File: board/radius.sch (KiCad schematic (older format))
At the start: 11 parts, among them IC1 STM8S003F3P, P1 CONN_01X04, P2 CONN_01X10, U1 CH340G, U2 LM2931AZ-3.3/5.0, Y1 Crystal

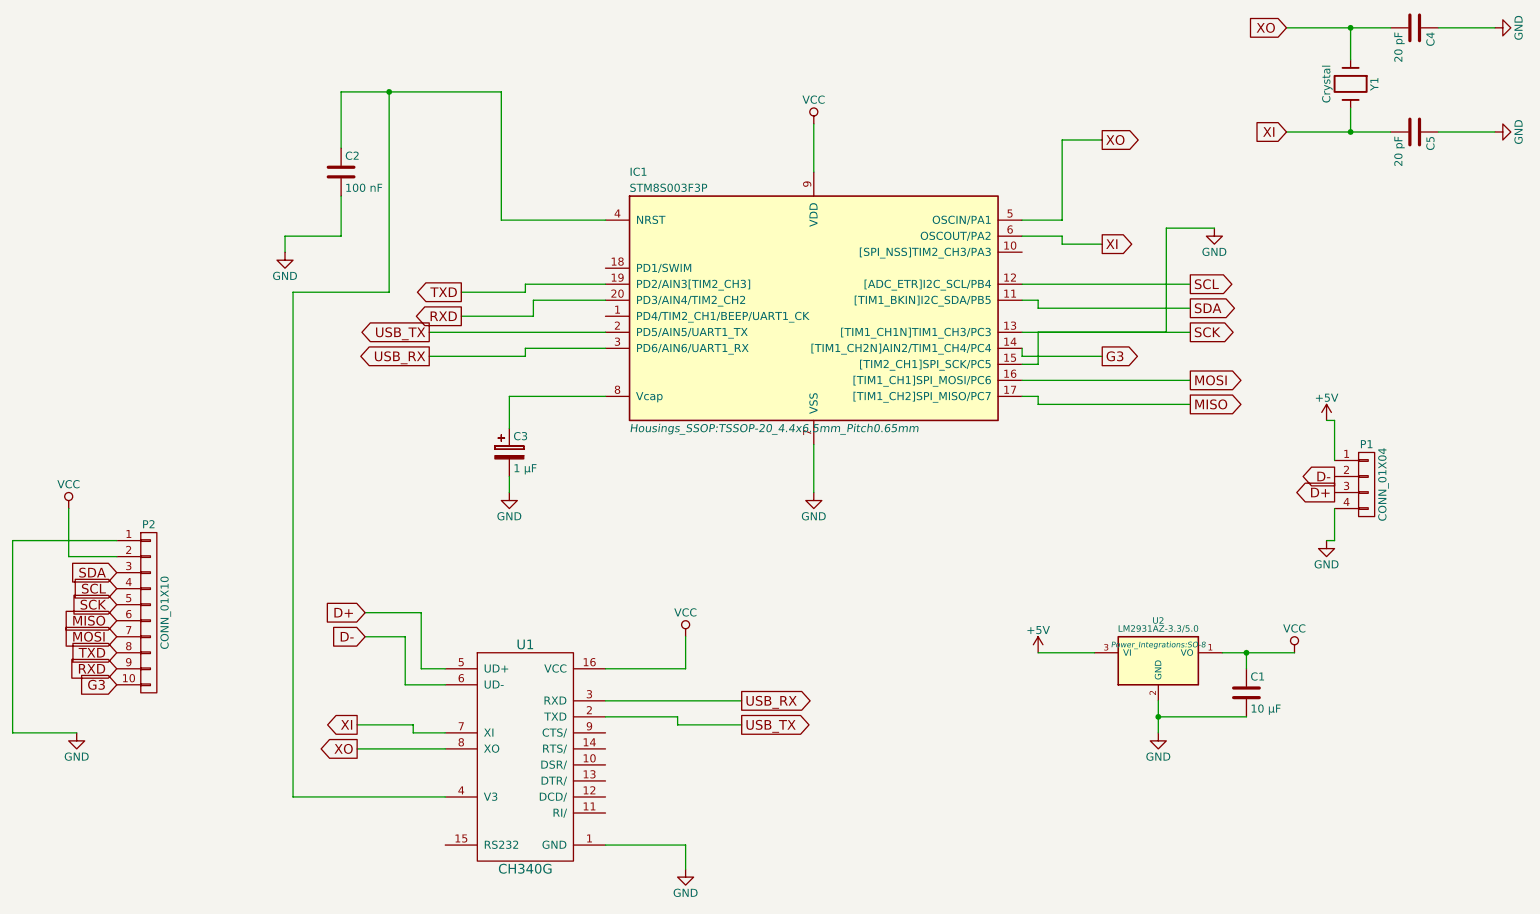
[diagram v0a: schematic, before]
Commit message: Support SWIM connector.
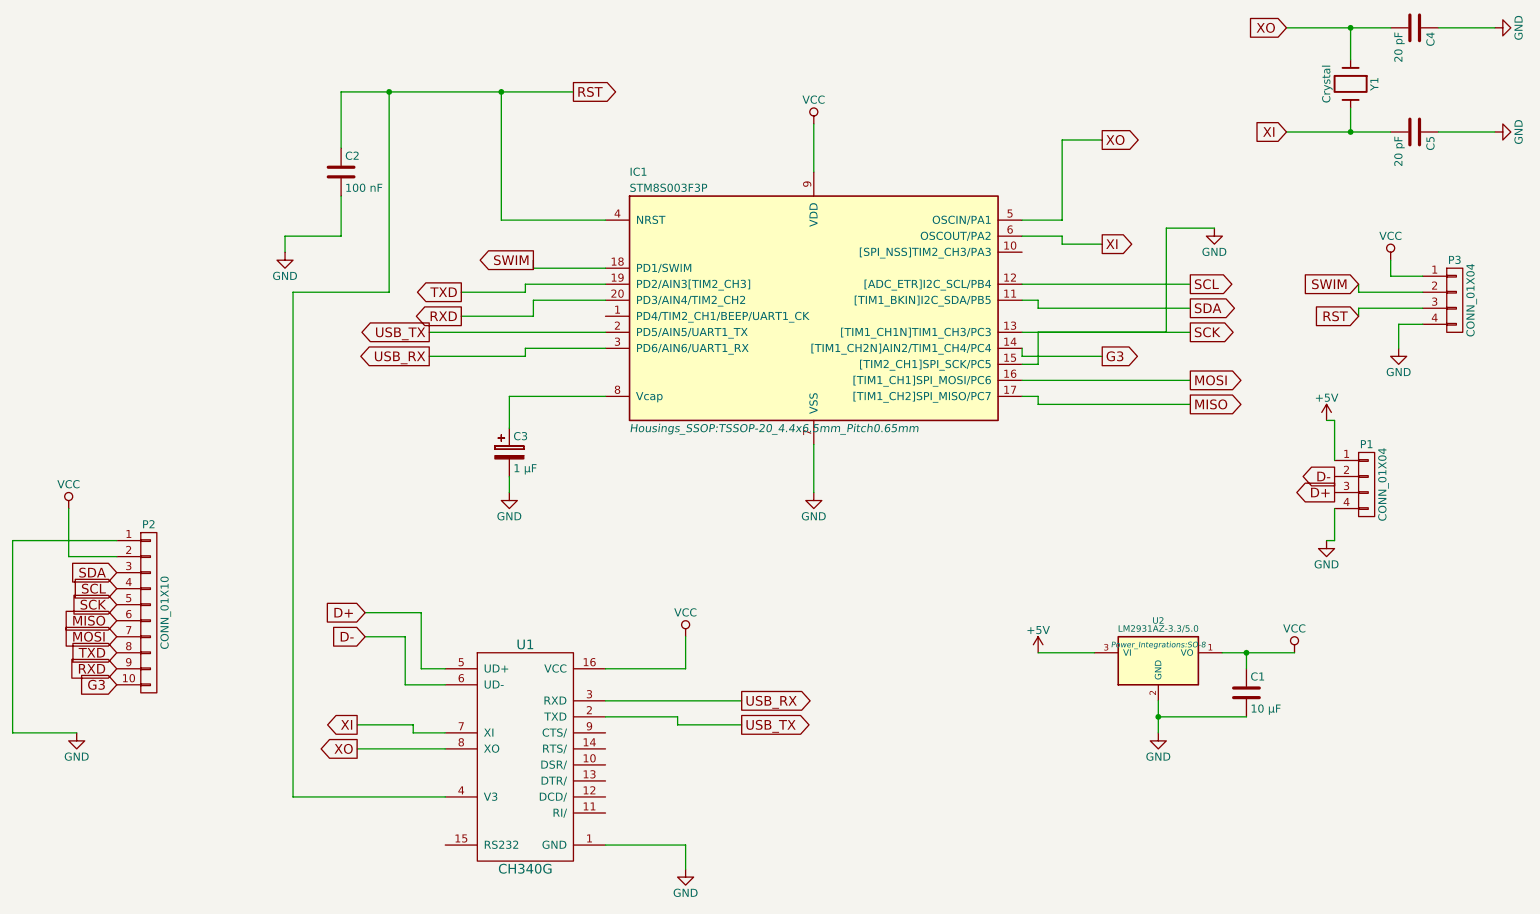
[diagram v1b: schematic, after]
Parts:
- added P3: CONN_01X04, conn-2mm:CONN-2MM-M-1x4, symbol CONN_01X04
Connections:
- net GND: now also P3.4 (P4)
- net VCC: now also P3.1 (P1)
- net SWIM: now reaches IC1.18 (PD1/SWIM)
- net SWIM: now also P3.2 (P2)
- net RST: now reaches C2.1, IC1.4 (NRST), U1.4 (V3)
- net RST: now also P3.3 (P3)
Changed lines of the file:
@@
 $EndComp
 $Comp
-L GND #PWR01
+L GND #PWR4
 U 1 1 557FA54B
 P 4100 3900
-F 0 "#PWR01" H 4100 3650 50  0001 C CNN
+F 0 "#PWR4" H 4100 3650 50  0001 C CNN
 F 1 "GND" H 4100 3750 50  0000 C CNN
 F 2 "" H 4100 3900 60  0000 C CNN
@@
 $EndComp
 $Comp
-L GND #PWR02
+L GND #PWR8
 U 1 1 557FB0DB
 P 6000 3900
-F 0 "#PWR02" H 6000 3650 50  0001 C CNN
+F 0 "#PWR8" H 6000 3650 50  0001 C CNN
 F 1 "GND" H 6000 3750 50  0000 C CNN
 F 2 "" H 6000 3900 60  0000 C CNN
@@
 $EndComp
 $Comp
-L GND #PWR03
+L GND #PWR3
 U 1 1 557FB357
 P 2700 2400
-F 0 "#PWR03" H 2700 2150 50  0001 C CNN
+F 0 "#PWR3" H 2700 2150 50  0001 C CNN
 F 1 "GND" H 2700 2250 50  0000 C CNN
 F 2 "" H 2700 2400 60  0000 C CNN
@@
 $EndComp
 $Comp
-L GND #PWR04
+L GND #PWR17
 U 1 1 557FB5FD
 P 10250 1000
-F 0 "#PWR04" H 10250 750 50  0001 C CNN
+F 0 "#PWR17" H 10250 750 50  0001 C CNN
 F 1 "GND" H 10250 850 50  0000 C CNN
 F 2 "" H 10250 1000 60  0000 C CNN
@@
 $EndComp
 $Comp
-L GND #PWR05
+L GND #PWR18
 U 1 1 557FB61D
 P 10250 1650
-F 0 "#PWR05" H 10250 1400 50  0001 C CNN
+F 0 "#PWR18" H 10250 1400 50  0001 C CNN
 F 1 "GND" H 10250 1500 50  0000 C CNN
 F 2 "" H 10250 1650 60  0000 C CNN
@@
 $EndComp
 $Comp
-L GND #PWR06
+L GND #PWR6
 U 1 1 557FBE42
 P 5200 6250
-F 0 "#PWR06" H 5200 6000 50  0001 C CNN
+F 0 "#PWR6" H 5200 6000 50  0001 C CNN
 F 1 "GND" H 5200 6100 50  0000 C CNN
 F 2 "" H 5200 6250 60  0000 C CNN
@@
 $EndComp
 $Comp
-L VCC #PWR07
+L VCC #PWR5
 U 1 1 557FBEB7
 P 5200 4800
-F 0 "#PWR07" H 5200 4650 50  0001 C CNN
+F 0 "#PWR5" H 5200 4650 50  0001 C CNN
 F 1 "VCC" H 5200 4950 50  0000 C CNN
 F 2 "" H 5200 4800 60  0000 C CNN
@@
 	3050 1750 3050 1400
 Wire Wire Line
-	3050 1400 4050 1400
+	3050 1400 4500 1400
 Wire Wire Line
 	4050 1400 4050 2200
@@
 $EndComp
 $Comp
-L VCC #PWR08
+L VCC #PWR7
 U 1 1 557FCD3A
 P 6000 1600
-F 0 "#PWR08" H 6000 1450 50  0001 C CNN
+F 0 "#PWR7" H 6000 1450 50  0001 C CNN
 F 1 "VCC" H 6000 1750 50  0000 C CNN
 F 2 "" H 6000 1600 60  0000 C CNN
@@
 $EndComp
 $Comp
-L +5V #PWR09
+L +5V #PWR9
 U 1 1 557FCD60
 P 7400 4900
-F 0 "#PWR09" H 7400 4750 50  0001 C CNN
+F 0 "#PWR9" H 7400 4750 50  0001 C CNN
 F 1 "+5V" H 7400 5040 50  0000 C CNN
 F 2 "" H 7400 4900 60  0000 C CNN
@@
 $EndComp
 $Comp
-L VCC #PWR010
+L VCC #PWR12
 U 1 1 557FCD86
 P 9000 4900
-F 0 "#PWR010" H 9000 4750 50  0001 C CNN
+F 0 "#PWR12" H 9000 4750 50  0001 C CNN
 F 1 "VCC" H 9000 5050 50  0000 C CNN
 F 2 "" H 9000 4900 60  0000 C CNN
@@
 $EndComp
 $Comp
-L GND #PWR011
+L GND #PWR10
 U 1 1 557FCDAC
 P 8150 5400
-F 0 "#PWR011" H 8150 5150 50  0001 C CNN
+F 0 "#PWR10" H 8150 5150 50  0001 C CNN
 F 1 "GND" H 8150 5250 50  0000 C CNN
 F 2 "" H 8150 5400 60  0000 C CNN
@@
 D+
 $Comp
-L GND #PWR012
+L GND #PWR14
 U 1 1 557FD427
 P 9200 4200
-F 0 "#PWR012" H 9200 3950 50  0001 C CNN
+F 0 "#PWR14" H 9200 3950 50  0001 C CNN
 F 1 "GND" H 9200 4050 50  0000 C CNN
 F 2 "" H 9200 4200 60  0000 C CNN
@@
 $EndComp
 $Comp
-L +5V #PWR013
+L +5V #PWR13
 U 1 1 557FD44F
 P 9200 3450
-F 0 "#PWR013" H 9200 3300 50  0001 C CNN
+F 0 "#PWR13" H 9200 3300 50  0001 C CNN
 F 1 "+5V" H 9200 3590 50  0000 C CNN
 F 2 "" H 9200 3450 60  0000 C CNN
@@
 $EndComp
 $Comp
-L GND #PWR014
+L GND #PWR2
 U 1 1 557FD669
 P 1400 5400
-F 0 "#PWR014" H 1400 5150 50  0001 C CNN
+F 0 "#PWR2" H 1400 5150 50  0001 C CNN
 F 1 "GND" H 1400 5250 50  0000 C CNN
 F 2 "" H 1400 5400 60  0000 C CNN
@@
 $EndComp
 $Comp
-L VCC #PWR015
+L VCC #PWR1
 U 1 1 557FD693
 P 1350 4000
-F 0 "#PWR015" H 1350 3850 50  0001 C CNN
+F 0 "#PWR1" H 1350 3850 50  0001 C CNN
 F 1 "VCC" H 1350 4150 50  0000 C CNN
 F 2 "" H 1350 4000 60  0000 C CNN
@@
 	8200 2250 8500 2250
 $Comp
-L GND #PWR016
+L GND #PWR11
 U 1 1 559188A2
 P 8500 2250
-F 0 "#PWR016" H 8500 2000 50  0001 C CNN
+F 0 "#PWR11" H 8500 2000 50  0001 C CNN
 F 1 "GND" H 8500 2100 50  0000 C CNN
 F 2 "" H 8500 2250 60  0000 C CNN
@@
 	1    0    0    -1
 $EndComp
+Connection ~ 4050 1400
+Text GLabel 4500 1400 2    60   Output ~ 0
+RST
+$Comp
+L CONN_01X04 P3
+U 1 1 55AC5BB9
+P 10000 2700
+F 0 "P3" H 10000 2950 50  0000 C CNN
+F 1 "CONN_01X04" V 10100 2700 50  0000 C CNN
+F 2 "conn-2mm:CONN-2MM-M-1x4" H 10000 2700 60  0001 C CNN
+F 3 "" H 10000 2700 60  0000 C CNN
+	1    10000 2700
+	1    0    0    -1
+$EndComp
+$Comp
+L GND #PWR16
+U 1 1 55AC5C37
+P 9650 3000
+F 0 "#PWR16" H 9650 2750 50  0001 C CNN
+F 1 "GND" H 9650 2850 50  0000 C CNN
+F 2 "" H 9650 3000 60  0000 C CNN
+F 3 "" H 9650 3000 60  0000 C CNN
+	1    9650 3000
+	1    0    0    -1
+$EndComp
+$Comp
+L VCC #PWR15
+U 1 1 55AC5C63
+P 9600 2450
+F 0 "#PWR15" H 9600 2300 50  0001 C CNN
+F 1 "VCC" H 9600 2600 50  0000 C CNN
+F 2 "" H 9600 2450 60  0000 C CNN
+F 3 "" H 9600 2450 60  0000 C CNN
+	1    9600 2450
+	1    0    0    -1
+$EndComp
+Wire Wire Line
+	9800 2550 9600 2550
+Wire Wire Line
+	9600 2550 9600 2450
+Wire Wire Line
+	9800 2850 9650 2850
+Wire Wire Line
+	9650 2850 9650 3000
+Text GLabel 9400 2600 0    60   Input ~ 0
+SWIM
+Text GLabel 9400 2800 0    60   Input ~ 0
+RST
+Wire Wire Line
+	9800 2750 9400 2750
+Wire Wire Line
+	9400 2750 9400 2800
+Wire Wire Line
+	9800 2650 9400 2650
+Wire Wire Line
+	9400 2650 9400 2600
+Text GLabel 4250 2450 0    60   Output ~ 0
+SWIM
+Wire Wire Line
+	4700 2500 4250 2500
+Wire Wire Line
+	4250 2500 4250 2450
 $EndSCHEMATC

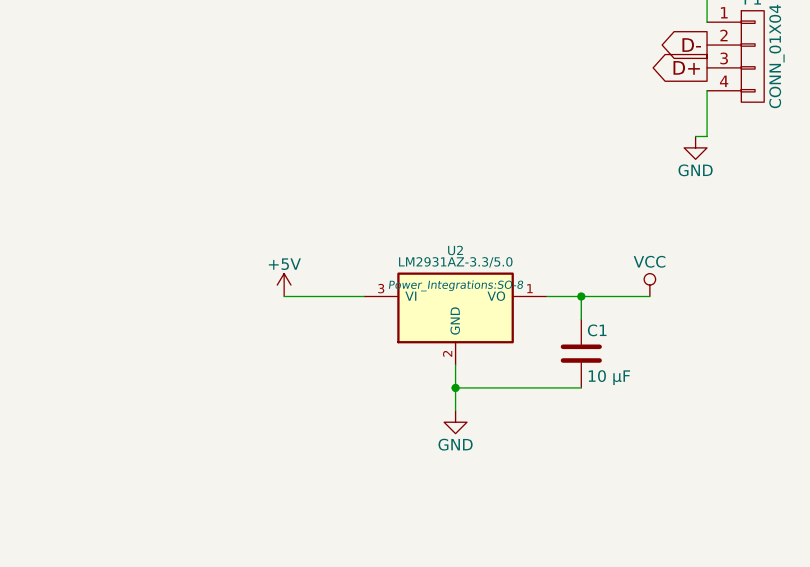
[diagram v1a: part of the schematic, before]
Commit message: Corrects power adapter pinout.
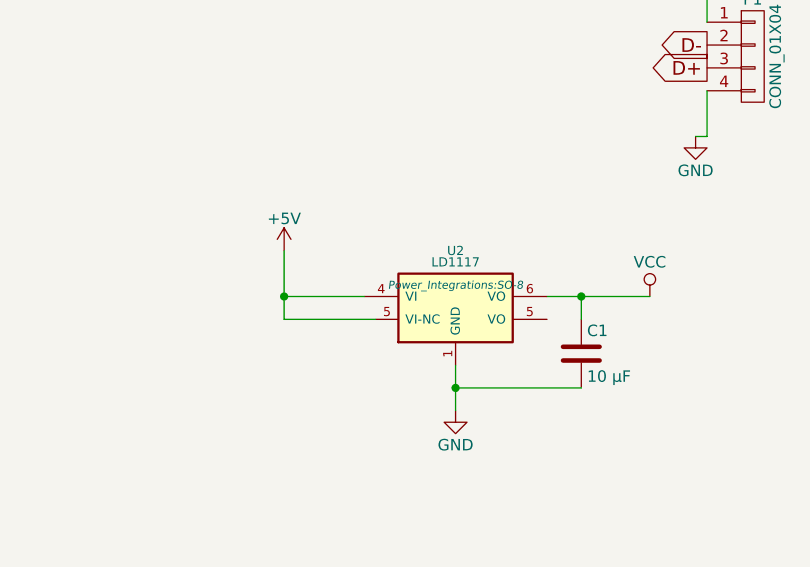
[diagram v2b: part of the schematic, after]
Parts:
- removed U2: LM2931AZ-3.3/5.0, Power_Integrations:SO-8, symbol LM2931AZ-3.3/5.0
- added U2: LD1117, Power_Integrations:SO-8, symbol LD1117
- P3: footprint conn-2mm:CONN-2MM-M-1x4 -> radius:RADIUS-CONN-2MM-M-1x4
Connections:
- net +5V: now also U2.4 (VI), U2.5 (VO)
- net GND: now also U2.1 (GND)
- net VCC: now also U2.6 (VO)
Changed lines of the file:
@@
 LIBS:stm8
 LIBS:serial_interface
-LIBS:radius-cache
+LIBS:radius
 EELAYER 25 0
 EELAYER END
@@
 $EndComp
 $Comp
-L GND #PWR4
+L GND #PWR01
 U 1 1 557FA54B
 P 4100 3900
-F 0 "#PWR4" H 4100 3650 50  0001 C CNN
+F 0 "#PWR01" H 4100 3650 50  0001 C CNN
 F 1 "GND" H 4100 3750 50  0000 C CNN
 F 2 "" H 4100 3900 60  0000 C CNN
@@
 $EndComp
 $Comp
-L GND #PWR8
+L GND #PWR02
 U 1 1 557FB0DB
 P 6000 3900
-F 0 "#PWR8" H 6000 3650 50  0001 C CNN
+F 0 "#PWR02" H 6000 3650 50  0001 C CNN
 F 1 "GND" H 6000 3750 50  0000 C CNN
 F 2 "" H 6000 3900 60  0000 C CNN
@@
 $EndComp
 $Comp
-L GND #PWR3
+L GND #PWR03
 U 1 1 557FB357
 P 2700 2400
-F 0 "#PWR3" H 2700 2150 50  0001 C CNN
+F 0 "#PWR03" H 2700 2150 50  0001 C CNN
 F 1 "GND" H 2700 2250 50  0000 C CNN
 F 2 "" H 2700 2400 60  0000 C CNN
@@
 $EndComp
 $Comp
-L GND #PWR17
+L GND #PWR04
 U 1 1 557FB5FD
 P 10250 1000
-F 0 "#PWR17" H 10250 750 50  0001 C CNN
+F 0 "#PWR04" H 10250 750 50  0001 C CNN
 F 1 "GND" H 10250 850 50  0000 C CNN
 F 2 "" H 10250 1000 60  0000 C CNN
@@
 $EndComp
 $Comp
-L GND #PWR18
+L GND #PWR05
 U 1 1 557FB61D
 P 10250 1650
-F 0 "#PWR18" H 10250 1400 50  0001 C CNN
+F 0 "#PWR05" H 10250 1400 50  0001 C CNN
 F 1 "GND" H 10250 1500 50  0000 C CNN
 F 2 "" H 10250 1650 60  0000 C CNN
@@
 $EndComp
 $Comp
-L GND #PWR6
+L GND #PWR06
 U 1 1 557FBE42
 P 5200 6250
-F 0 "#PWR6" H 5200 6000 50  0001 C CNN
+F 0 "#PWR06" H 5200 6000 50  0001 C CNN
 F 1 "GND" H 5200 6100 50  0000 C CNN
 F 2 "" H 5200 6250 60  0000 C CNN
@@
 $EndComp
 $Comp
-L VCC #PWR5
+L VCC #PWR07
 U 1 1 557FBEB7
 P 5200 4800
-F 0 "#PWR5" H 5200 4650 50  0001 C CNN
+F 0 "#PWR07" H 5200 4650 50  0001 C CNN
 F 1 "VCC" H 5200 4950 50  0000 C CNN
 F 2 "" H 5200 4800 60  0000 C CNN
@@
 	3450 4800 3200 4800
 $Comp
-L LM2931AZ-3.3/5.0 U2
-U 1 1 557FCB91
-P 8150 4950
-F 0 "U2" H 8150 5200 40  0000 C CNN
-F 1 "LM2931AZ-3.3/5.0" H 8150 5150 40  0000 C CNN
-F 2 "Power_Integrations:SO-8" H 8150 5050 35  0000 C CIN
-F 3 "" H 8150 4950 60  0000 C CNN
-	1    8150 4950
-	1    0    0    -1
-$EndComp
-$Comp
-L VCC #PWR7
+L VCC #PWR08
 U 1 1 557FCD3A
 P 6000 1600
-F 0 "#PWR7" H 6000 1450 50  0001 C CNN
+F 0 "#PWR08" H 6000 1450 50  0001 C CNN
 F 1 "VCC" H 6000 1750 50  0000 C CNN
 F 2 "" H 6000 1600 60  0000 C CNN
@@
 $EndComp
 $Comp
-L +5V #PWR9
+L +5V #PWR09
 U 1 1 557FCD60
-P 7400 4900
-F 0 "#PWR9" H 7400 4750 50  0001 C CNN
-F 1 "+5V" H 7400 5040 50  0000 C CNN
-F 2 "" H 7400 4900 60  0000 C CNN
-F 3 "" H 7400 4900 60  0000 C CNN
-	1    7400 4900
-	1    0    0    -1
-$EndComp
-$Comp
-L VCC #PWR12
+P 7400 4700
+F 0 "#PWR09" H 7400 4550 50  0001 C CNN
+F 1 "+5V" H 7400 4840 50  0000 C CNN
+F 2 "" H 7400 4700 60  0000 C CNN
+F 3 "" H 7400 4700 60  0000 C CNN
+	1    7400 4700
+	1    0    0    -1
+$EndComp
+$Comp
+L VCC #PWR010
 U 1 1 557FCD86
 P 9000 4900
-F 0 "#PWR12" H 9000 4750 50  0001 C CNN
+F 0 "#PWR010" H 9000 4750 50  0001 C CNN
 F 1 "VCC" H 9000 5050 50  0000 C CNN
 F 2 "" H 9000 4900 60  0000 C CNN
@@
 $EndComp
 $Comp
-L GND #PWR10
+L GND #PWR011
 U 1 1 557FCDAC
 P 8150 5400
-F 0 "#PWR10" H 8150 5150 50  0001 C CNN
+F 0 "#PWR011" H 8150 5150 50  0001 C CNN
 F 1 "GND" H 8150 5250 50  0000 C CNN
 F 2 "" H 8150 5400 60  0000 C CNN
@@
 	1    0    0    -1
 $EndComp
-Wire Wire Line
-	7400 4900 7750 4900
 Wire Wire Line
 	8550 4900 9000 4900
@@
 D+
 $Comp
-L GND #PWR14
+L GND #PWR012
 U 1 1 557FD427
 P 9200 4200
-F 0 "#PWR14" H 9200 3950 50  0001 C CNN
+F 0 "#PWR012" H 9200 3950 50  0001 C CNN
 F 1 "GND" H 9200 4050 50  0000 C CNN
 F 2 "" H 9200 4200 60  0000 C CNN
@@
 $EndComp
 $Comp
-L +5V #PWR13
+L +5V #PWR013
 U 1 1 557FD44F
 P 9200 3450
-F 0 "#PWR13" H 9200 3300 50  0001 C CNN
+F 0 "#PWR013" H 9200 3300 50  0001 C CNN
 F 1 "+5V" H 9200 3590 50  0000 C CNN
 F 2 "" H 9200 3450 60  0000 C CNN
@@
 $EndComp
 $Comp
-L GND #PWR2
+L GND #PWR014
 U 1 1 557FD669
 P 1400 5400
-F 0 "#PWR2" H 1400 5150 50  0001 C CNN
+F 0 "#PWR014" H 1400 5150 50  0001 C CNN
 F 1 "GND" H 1400 5250 50  0000 C CNN
 F 2 "" H 1400 5400 60  0000 C CNN
@@
 $EndComp
 $Comp
-L VCC #PWR1
+L VCC #PWR015
 U 1 1 557FD693
 P 1350 4000
-F 0 "#PWR1" H 1350 3850 50  0001 C CNN
+F 0 "#PWR015" H 1350 3850 50  0001 C CNN
 F 1 "VCC" H 1350 4150 50  0000 C CNN
 F 2 "" H 1350 4000 60  0000 C CNN
@@
 	8200 2250 8500 2250
 $Comp
-L GND #PWR11
+L GND #PWR016
 U 1 1 559188A2
 P 8500 2250
-F 0 "#PWR11" H 8500 2000 50  0001 C CNN
+F 0 "#PWR016" H 8500 2000 50  0001 C CNN
 F 1 "GND" H 8500 2100 50  0000 C CNN
 F 2 "" H 8500 2250 60  0000 C CNN
@@
 F 0 "P3" H 10000 2950 50  0000 C CNN
 F 1 "CONN_01X04" V 10100 2700 50  0000 C CNN
-F 2 "conn-2mm:CONN-2MM-M-1x4" H 10000 2700 60  0001 C CNN
+F 2 "radius:RADIUS-CONN-2MM-M-1x4" H 10000 2700 60  0001 C CNN
 F 3 "" H 10000 2700 60  0000 C CNN
 	1    10000 2700
@@
 $EndComp
 $Comp
-L GND #PWR16
+L GND #PWR017
 U 1 1 55AC5C37
 P 9650 3000
-F 0 "#PWR16" H 9650 2750 50  0001 C CNN
+F 0 "#PWR017" H 9650 2750 50  0001 C CNN
 F 1 "GND" H 9650 2850 50  0000 C CNN
 F 2 "" H 9650 3000 60  0000 C CNN
@@
 $EndComp
 $Comp
-L VCC #PWR15
+L VCC #PWR018
 U 1 1 55AC5C63
 P 9600 2450
-F 0 "#PWR15" H 9600 2300 50  0001 C CNN
+F 0 "#PWR018" H 9600 2300 50  0001 C CNN
 F 1 "VCC" H 9600 2600 50  0000 C CNN
 F 2 "" H 9600 2450 60  0000 C CNN
@@
 Wire Wire Line
 	4250 2500 4250 2450
+Wire Wire Line
+	7800 5000 7400 5000
+Wire Wire Line
+	7400 5000 7400 4700
+Wire Wire Line
+	7750 4900 7400 4900
+Connection ~ 7400 4900
+$Comp
+L LD1117 U2
+U 1 1 55AC7D39
+P 8150 4950
+F 0 "U2" H 8150 5200 40  0000 C CNN
+F 1 "LD1117" H 8150 5150 40  0000 C CNN
+F 2 "Power_Integrations:SO-8" H 8150 5050 35  0000 C CIN
+F 3 "" H 8150 4950 60  0000 C CNN
+	1    8150 4950
+	1    0    0    -1
+$EndComp
 $EndSCHEMATC
